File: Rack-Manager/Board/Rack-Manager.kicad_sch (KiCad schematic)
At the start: 0 parts

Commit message: Added RS485 protection data as task describe and fixed stuff around
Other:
- sheet USB-PD Controller renamed USB-C
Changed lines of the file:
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@@
-	(text "Note"
-		(exclude_from_sim no)
-		(at 438.15 48.26 0)
-		(effects
-			(font
-				(size 2.54 2.54)
-				(thickness 0.508)
-				(bold yes)
-				(color 194 0 0 1)
-			)
-		)
-	)
 	(text "Note"
 		(exclude_from_sim no)
@@
 		(exclude_from_sim no)
 		(at 317.5 50.8 0)
-		(size 38.1 12.7)
-		(margins 0.9525 0.9525 0.9525 0.9525)
-		(stroke
-			(width 0.508)
-			(type dot)
-			(color 194 0 0 1)
-		)
-		(fill
-			(type color)
-			(color 255 165 169 1)
-		)
-		(effects
-			(font
-				(size 1.27 1.27)
-			)
-		)
-	)
-	(text_box "Varistors and MOV data missing"
-		(exclude_from_sim no)
-		(at 419.1 50.8 0)
 		(size 38.1 12.7)
 		(margins 0.9525 0.9525 0.9525 0.9525)
@@
 			(color 255 255 194 1.0000)
 		)
-		(property "Sheetname" "USB-PD Controller"
+		(property "Sheetname" "USB-C"
 			(at 228.6 37.3884 0)
 			(effects

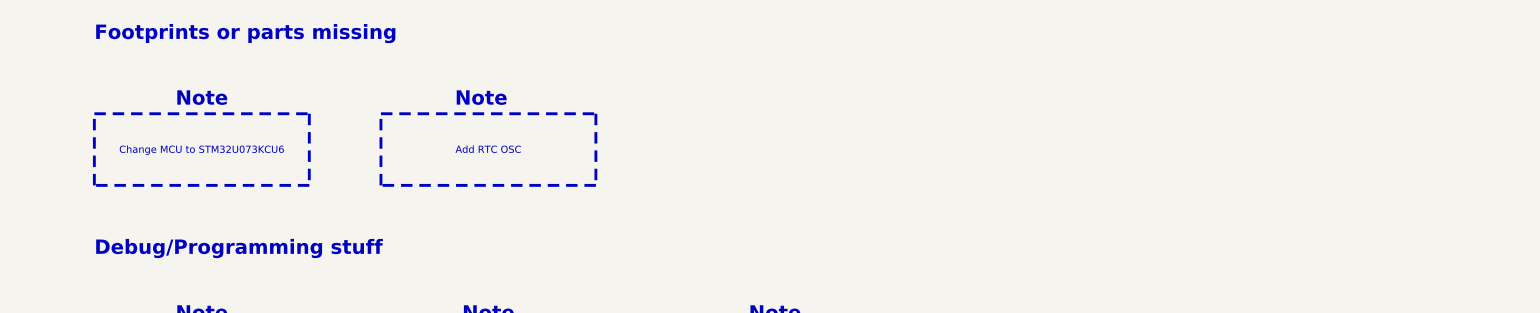
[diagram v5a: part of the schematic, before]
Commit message: Found some error or missing stuff and noted on the main sheet
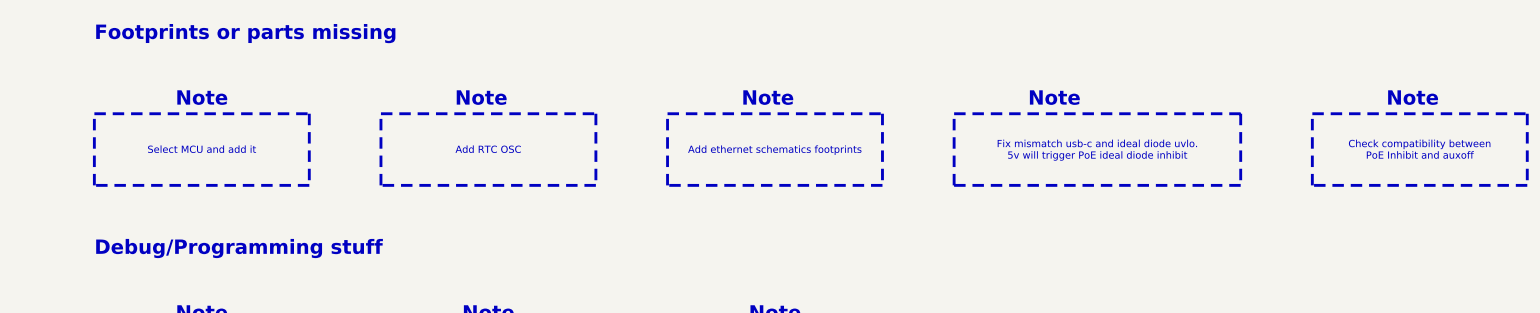
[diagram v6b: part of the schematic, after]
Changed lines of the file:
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@@
+	(text "Note"
+		(exclude_from_sim no)
+		(at 551.18 48.26 0)
+		(effects
+			(font
+				(size 2.54 2.54)
+				(thickness 0.508)
+				(bold yes)
+				(color 194 0 0 1)
+			)
+		)
+	)
 	(text "Note"
 		(exclude_from_sim no)
@@
 	(text "Note"
 		(exclude_from_sim no)
+		(at 487.68 48.26 0)
+		(effects
+			(font
+				(size 2.54 2.54)
+				(thickness 0.508)
+				(bold yes)
+				(color 194 0 0 1)
+			)
+		)
+	)
+	(text "Note"
+		(exclude_from_sim no)
 		(at 438.15 86.36 0)
 		(effects
@@
 	(text "Note"
 		(exclude_from_sim no)
+		(at 436.88 48.26 0)
+		(effects
+			(font
+				(size 2.54 2.54)
+				(thickness 0.508)
+				(bold yes)
+				(color 194 0 0 1)
+			)
+		)
+	)
+	(text "Note"
+		(exclude_from_sim no)
 		(at 387.35 86.36 0)
 		(effects
@@
 		)
 	)
+	(text_box "Check compatibility between\nPoE Inhibit and auxoff"
+		(exclude_from_sim no)
+		(at 533.4 50.8 0)
+		(size 38.1 12.7)
+		(margins 0.9525 0.9525 0.9525 0.9525)
+		(stroke
+			(width 0.508)
+			(type dot)
+			(color 194 0 0 1)
+		)
+		(fill
+			(type color)
+			(color 255 165 169 1)
+		)
+		(effects
+			(font
+				(size 1.27 1.27)
+			)
+		)
+	)
 	(text_box "Split all domains with 0R resistors"
 		(exclude_from_sim no)
@@
 		)
 	)
-	(text_box "Change MCU to STM32U073KCU6"
+	(text_box "Select MCU and add it"
 		(exclude_from_sim no)
 		(at 317.5 50.8 0)
@@
 		)
 	)
+	(text_box "Fix mismatch usb-c and ideal diode uvlo.\n5v will trigger PoE ideal diode inhibit"
+		(exclude_from_sim no)
+		(at 469.9 50.8 0)
+		(size 50.8 12.7)
+		(margins 0.9525 0.9525 0.9525 0.9525)
+		(stroke
+			(width 0.508)
+			(type dot)
+			(color 194 0 0 1)
+		)
+		(fill
+			(type color)
+			(color 255 165 169 1)
+		)
+		(effects
+			(font
+				(size 1.27 1.27)
+			)
+		)
+	)
 	(text_box "Use STLink standard debug/program connector"
 		(exclude_from_sim no)
@@
 		(size 38.1 12.7)
 		(margins 0.9525 0.9525 0.9525 0.9525)
+		(stroke
+			(width 0.508)
+			(type dot)
+			(color 194 0 0 1)
+		)
+		(fill
+			(type color)
+			(color 255 165 169 1)
+		)
+		(effects
+			(font
+				(size 1.27 1.27)
+			)
+		)
+	)
+	(text_box "Add ethernet schematics footprints"
+		(exclude_from_sim no)
+		(at 419.1 50.8 0)
+		(size 38.1 12.7)
+		(margins 0.9525 0.9525 0.9525 0.9525)

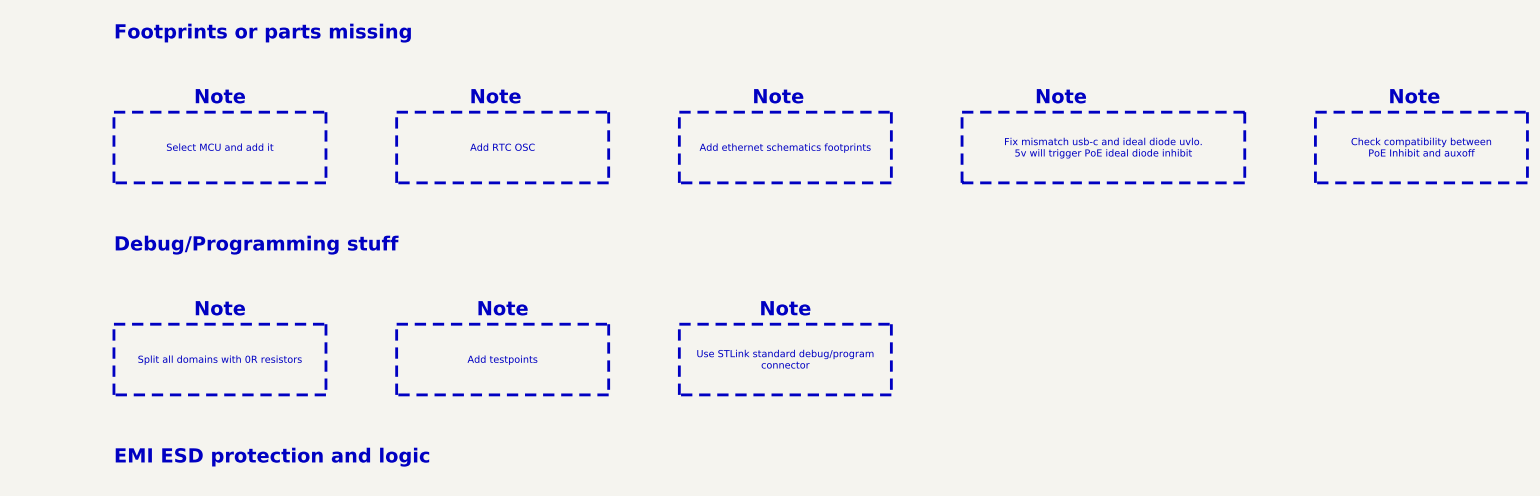
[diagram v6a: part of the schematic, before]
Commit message: Added MCU, Fixed USB-C PD Ideal Diode bug and updated the todo notes
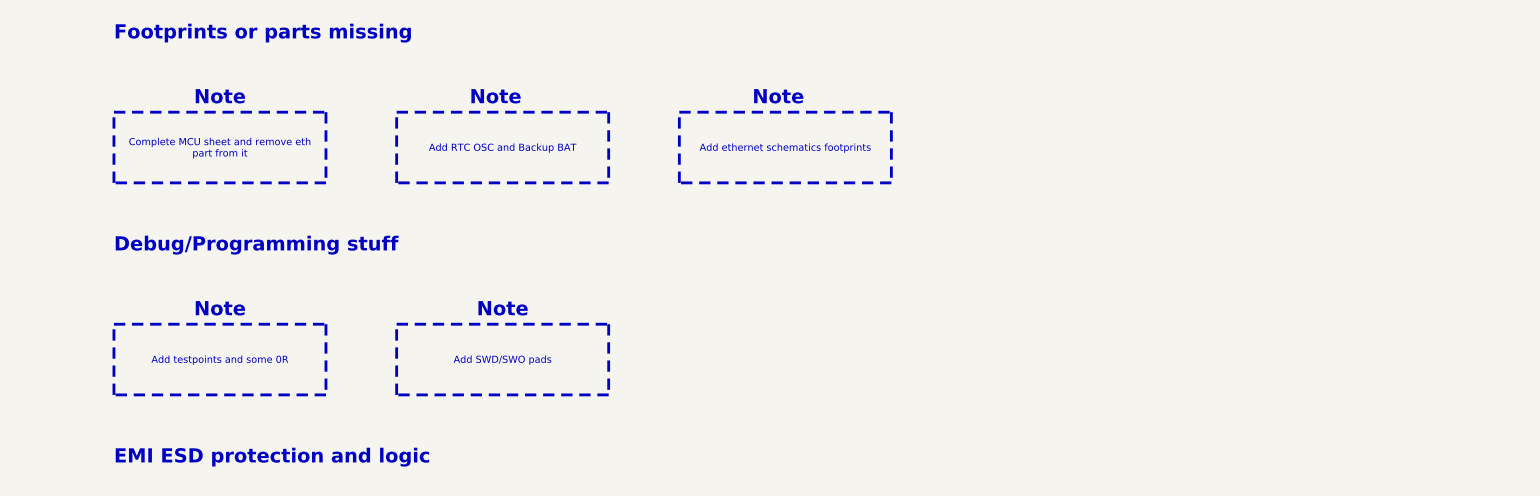
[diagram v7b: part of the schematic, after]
